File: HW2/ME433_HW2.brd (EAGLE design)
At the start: 100 x 80 mm, 22 parts, among them J1 USB-MB-H

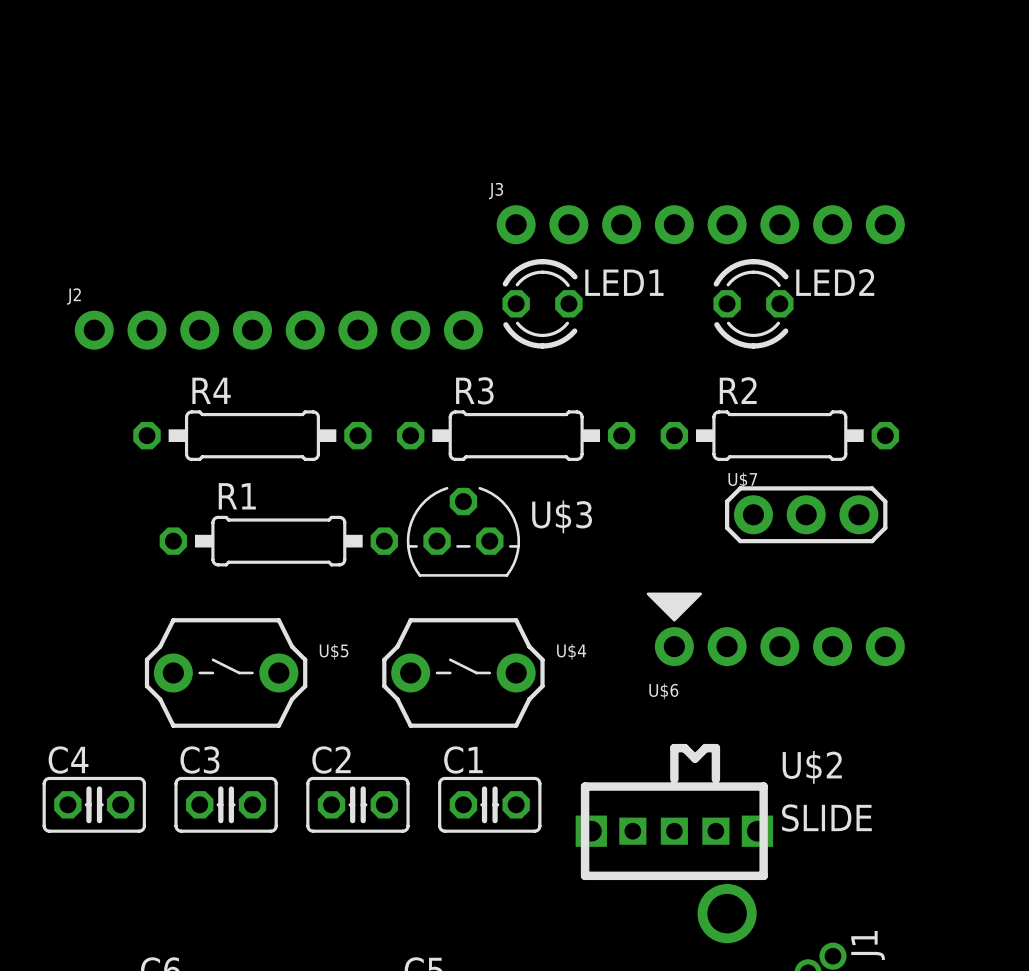
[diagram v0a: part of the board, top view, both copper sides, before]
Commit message: Redo HW2
Correct two mistakes in the schematic: (1) mirror the SLIDE to make
sure input and output connect to the right pin. (2) correct the pin
name and connection of PICKIT3
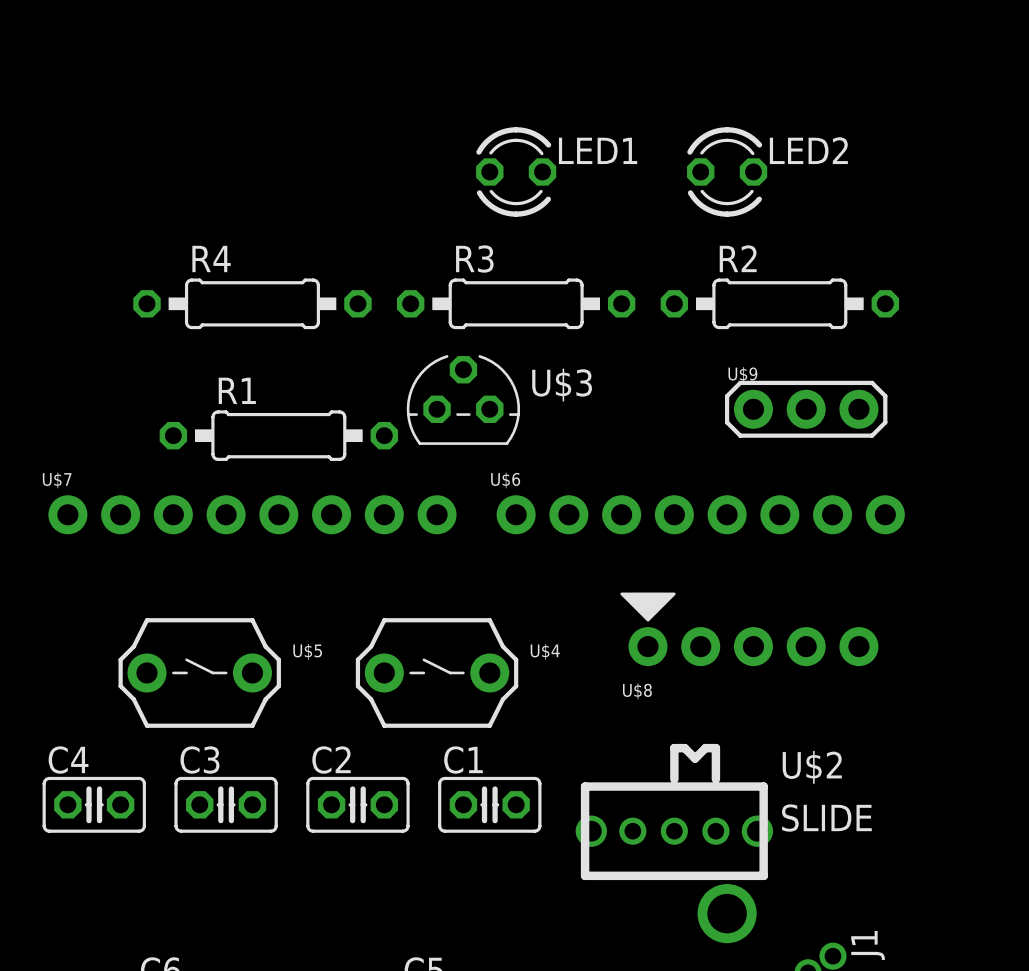
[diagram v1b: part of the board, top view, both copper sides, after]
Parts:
- removed J2, J3: (no value), ME433_HW2_1:1X08
- added U$8: PICKIT3, ME433_HW2:1X05
- added U$9: OSC, ME433_HW2:OSC
- J1: device ME433_HW2_1:USB-MB-H -> ME433_HW2:USB-MB-H
- LED1: value Red -> RED
- LED2: value Green -> GREEN
- U$1: device ME433_HW2_1:DIL28-3 -> ME433_HW2:DIL28-3
- U$2: device ME433_HW2_1:SLIDE -> ME433_HW2:SLIDE
- U$3: device ME433_HW2_1:TO92 -> ME433_HW2:TO92
- U$4: value Reset -> RESET; device ME433_HW2_1:PB -> ME433_HW2:PB
- U$5: value User -> USER; device ME433_HW2_1:PB -> ME433_HW2:PB
- U$6: value PICKIT3 -> CONN_08; device ME433_HW2_1:1X05 -> ME433_HW2:1X08
- U$7: value 8MHz -> CONN_08; device ME433_HW2_1:OSC -> ME433_HW2:1X08
- moved U$7 35.6 mm to (-53.3, 40.6)
- moved U$6 9.92 mm to (-31.8, 40.6)
- moved LED1 6.48 mm to (-31.8, 57.1)
- moved LED2 6.48 mm to (-21.6, 57.1)
- moved U$3 6.35 mm to (-34.3, 45.7)
- moved R2 6.35 mm to (-19.1, 50.8)
- moved R3 6.35 mm to (-31.8, 50.8)
- moved R4 6.35 mm to (-44.5, 50.8)
- moved R1 5.08 mm to (-43.2, 44.5)
- moved U$4 1.27 mm to (-35.6, 33.0)
- moved U$5 1.27 mm to (-47.0, 33.0)
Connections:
- removed net N$4: U$1.9, U$7.1
- removed net USER: R4.1, U$5.1
- new net N$6: U$1.9, U$9.1
- net +3V3: now also C3.1, R3.1, U$7.2, U$8.2; no longer C4.1, J3.2, R3.2, R4.2, U$6.5
- net +5V: now also C4.1, U$2.3, U$6.2; no longer C3.1, J2.2, U$2.1
- net A0: now also U$7.8; no longer J3.8
- net A1: now also U$7.7; no longer J3.7
- net A4/LED: now also U$7.3; no longer J3.3
- net B13: now also U$1.24, U$6.6; no longer J2.6
- net B14: now also U$1.25, U$6.7; no longer J2.7, U$1.24
- net B15: now also U$1.26, U$6.8; no longer J2.8, U$1.25
- net B2: now also U$7.6; no longer J3.6
- net B3: now also U$7.5; no longer J3.5
- net B4/USER: now also R3.2, U$4.1, U$7.4; no longer J3.4
- net B7: now also U$6.3; no longer J2.3
- net B8: now also U$6.4; no longer J2.4
- net B9: now also U$6.5; no longer J2.5
- net GND: now also R1.2, R2.2, U$7.1, U$8.3, U$9.2; no longer J2.1, J3.1, R1.1, R2.1, U$7.2
- net MCLR: now also R4.2, U$5.1, U$8.1; no longer R3.1, U$4.1, U$6.2
- net N$2: now also R1.1; no longer R1.2
- net N$3: now also R2.1; no longer R2.2
- net N$5: now also U$9.3; no longer U$7.3
- net PGC: now also U$8.5; no longer U$6.3
- net PGD: now also U$8.4; no longer U$6.4
